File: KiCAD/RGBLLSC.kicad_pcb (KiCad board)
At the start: 2 copper layers, 18 parts, among them P1 PICKIT3, Q1 FQP30N06L, Q2 FQP30N06L, Q3 FQP30N06L, SW1 SW_PUSH, U1 PIC12F1840

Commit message: Updated PCB Design and Schematic
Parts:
- removed P1: PICKIT3, Pin_Headers:Pin_Header_Straight_1x06
- added P3: MAIN OUT, User:Screw-Terminal-Thingy-5.08mm-0.2in, F.Cu at (104.6, 104.6)
- moved R10 77.0 mm to (119.4, 96.0), turned to 90 degrees
- moved R9 74.1 mm to (119.4, 90.2)
- moved U1 43.2 mm to (134.4, 95.2), turned to 180 degrees
- moved Q2 36.4 mm to (140.2, 113.8), turned to 180 degrees
- moved SW1 34.0 mm to (154.9, 93.5), turned to 90 degrees
- moved R7 33.7 mm to (163.8, 100.8)
- moved D1 33.0 mm to (167.6, 101.1)
- moved R8 32.0 mm to (152.7, 90.9), turned to 90 degrees
- moved C1 30.3 mm to (150.4, 95.8)
- moved R3 29.3 mm to (144.8, 110.0), turned to 90 degrees
- moved R4 26.0 mm to (142.7, 110.0)
- moved Q3 22.6 mm to (127.5, 113.8), turned to 180 degrees
- moved Q1 21.1 mm to (153.0, 113.8), turned to 180 degrees
- moved R5 12.5 mm to (132.1, 110.4), turned to 90 degrees
- moved R1 11.9 mm to (157.9, 110.2), turned to 90 degrees
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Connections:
- R10 pad 2: Net-(P3-Pad2) (its old number) -> Net-(P1-Pad5)
- R9 pad 2: Net-(P1-Pad5) -> Net-(P3-Pad6)
- U1 pad 5: Net-(P3-Pad2) (its old number) -> Net-(P3-Pad6)
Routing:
- net +3V3: track 0.00 -> 27.9 mm
- net GND: track 0.00 -> 17.6 mm
- net Net-(P1-Pad5): track 0.00 -> 7.42 mm
- net Net-(P3-Pad6): track 0.00 -> 7.12 mm
- net Net-(R1-Pad2): track 0.00 -> 3.11 mm
- net Net-(R3-Pad2): track 0.00 -> 3.08 mm
- net Net-(Q2-Pad1): track 0.00 -> 3.06 mm
- net Net-(Q1-Pad1): track 0.00 -> 2.81 mm
- net Net-(P1-Pad4): track 0.00 -> 2.75 mm
- net Net-(Q3-Pad1): track 0.00 -> 2.68 mm
- added copper zone on F.Cu, net GND
- added copper zone on F.Cu, net Net-(P3-Pad1)
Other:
- board outline added: 69.9 x 36.8 mm

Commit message: Finished PCB
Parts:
- added P2: PWR IN, User:Screw-Terminal-Thingy-3pin-3.5mm, F.Cu at (176.5, 104.1)
- P3: footprint User:Screw-Terminal-Thingy-5.08mm-0.2in -> User:Screw-Terminal-Thingy-6pin-3.5mm
- moved D1 14.7 mm to (171.2, 86.9)
- moved R7 14.4 mm to (167.4, 86.9), turned to 180 degrees
- moved SW1 12.7 mm to (167.4, 96.0)
- moved R8 11.5 mm to (163.8, 88.4), turned to 270 degrees
- moved U1 7.49 mm to (141.9, 95.4)
- moved R9 5.76 mm to (115.1, 94.0), turned to 180 degrees
- moved Q1 5.08 mm to (158.1, 113.8)
- moved Q2 5.08 mm to (145.3, 113.8)
- moved R1 5.08 mm to (162.9, 110.2)
- moved R2 5.08 mm to (160.7, 110.2)
- moved R3 5.08 mm to (149.9, 110.0)
- moved R4 5.08 mm to (147.8, 110.0)
- moved Q3 5.08 mm to (132.6, 113.8)
- moved R5 5.08 mm to (137.2, 110.4)
- moved R6 5.08 mm to (135.1, 110.4)
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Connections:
- C1 pad 2: +3V3 -> +5V
- R10 pad 1: +3V3 -> +5V
- R8 pad 1: +3V3 -> +5V
- R9 pad 1: +3V3 -> +5V
- SW1 pad 3: (no net) -> GND
- U1 pad 1: +3V3 -> +5V
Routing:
- net +5V: track 0.00 -> 95.4 mm
- net GND: track 17.6 -> 73.2 mm
- net Net-(R1-Pad2): track 3.11 -> 39.5 mm
- net +3V3: track 27.9 -> 0.00 mm
- net Net-(P1-Pad1): track 0.00 -> 26.5 mm
- net Net-(P1-Pad5): track 7.42 -> 33.6 mm
- net Net-(P3-Pad6): track 7.12 -> 29.9 mm
- net Net-(R3-Pad2): track 3.08 -> 7.15 mm
- net Net-(P1-Pad4): track 2.75 -> 6.74 mm
- net Net-(D1-Pad1): track 0.00 -> 2.31 mm
- added copper zone on F.Cu, net Net-(P3-Pad2)
- added copper zone on F.Cu, net Net-(P3-Pad3)

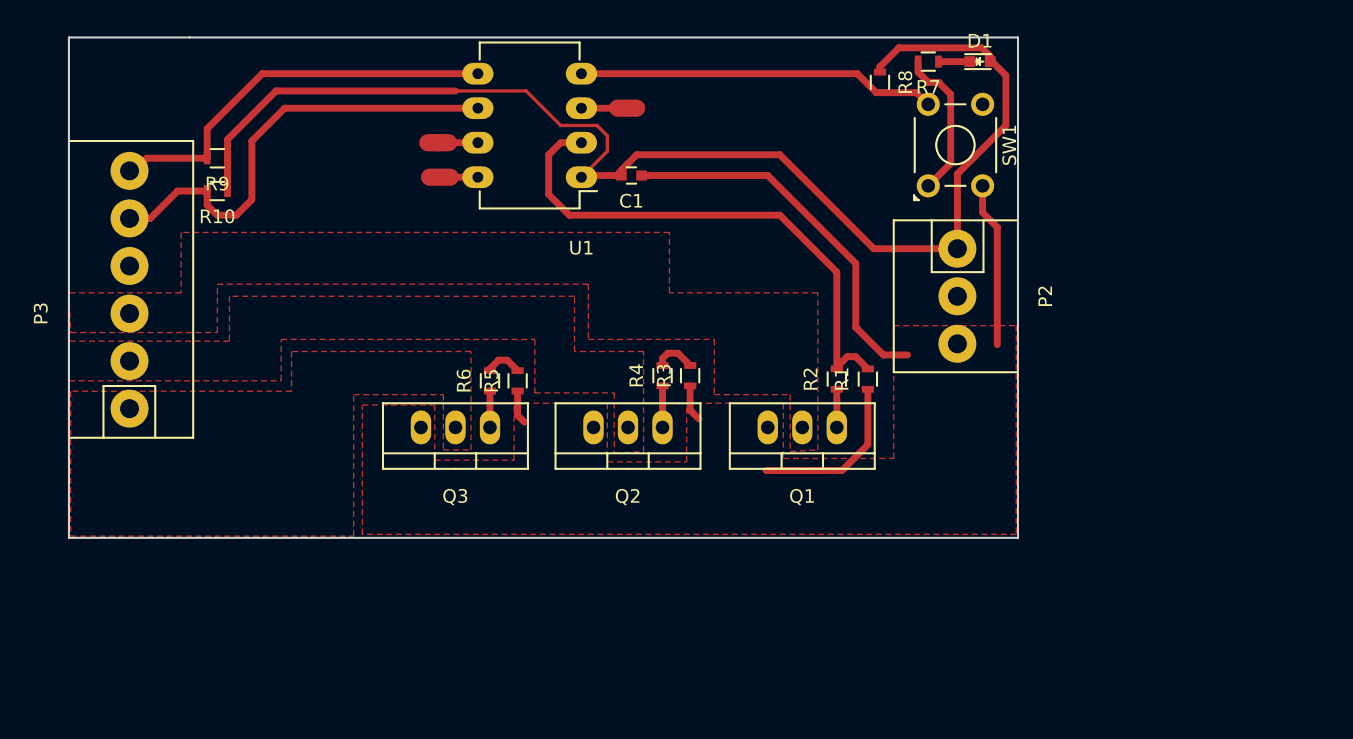
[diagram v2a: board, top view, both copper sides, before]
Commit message: Added OSHWA Logo to PCB
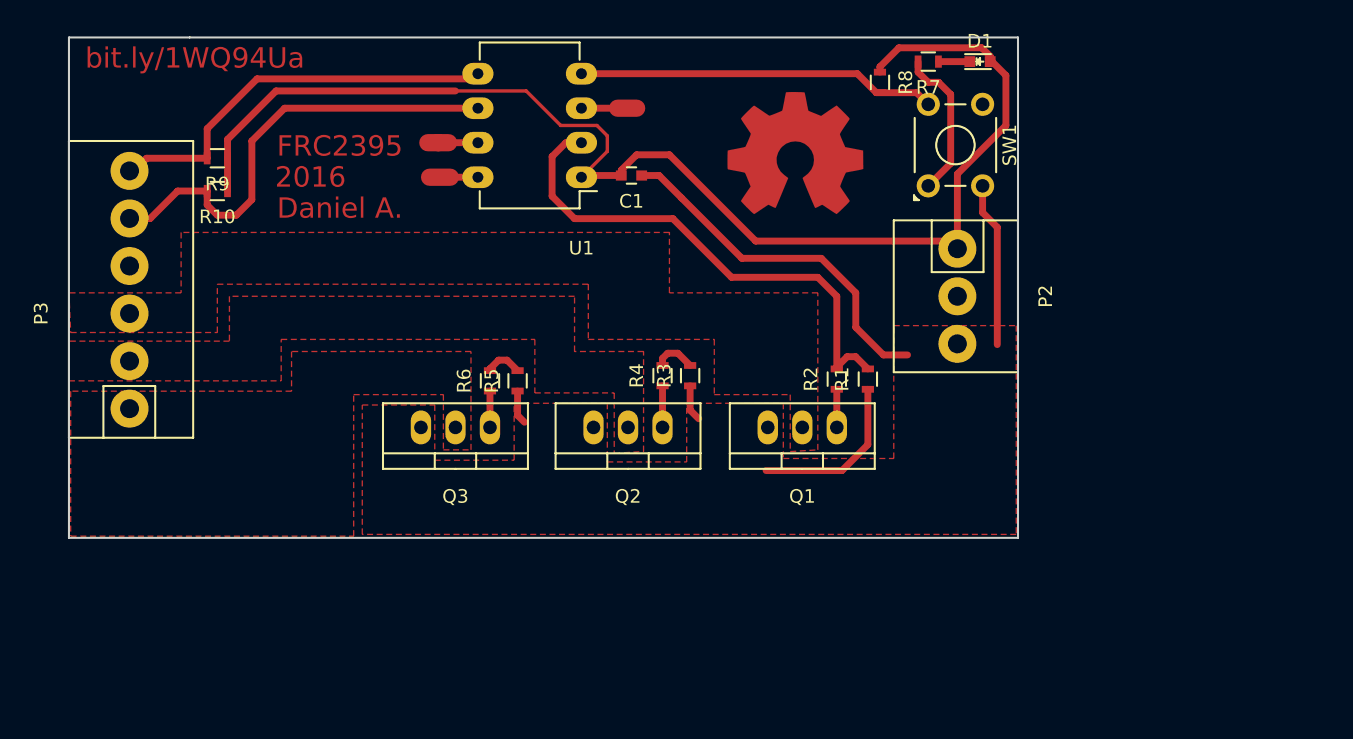
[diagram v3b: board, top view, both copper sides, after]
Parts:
- added G***: OSHW-logo_copper-back_10mm, OSHW-logo:OSHW-logo_copper-back_10mm, F.Cu at (157.6, 93.6)
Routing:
- net Net-(R1-Pad2): track 39.5 -> 38.0 mm
- net GND: track 73.2 -> 72.0 mm
- net +5V: track 95.4 -> 94.6 mm
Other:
- board text added: "2016"
- board text added: "Daniel A."
- board text added: "FRC2395"
- board text added: "bit.ly/1WQ94Ua"
